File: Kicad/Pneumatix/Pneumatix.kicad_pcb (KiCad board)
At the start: 2 copper layers, 34 x 59.4 mm, 25 parts, among them J1 Conn_01x06_Socket, J2 436500404, J3 142-0701-801, U1 E22-400T33S

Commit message: wip: pcb adjustements
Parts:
- removed R1: 1.5k, Resistor_SMD:R_0603_1608Metric
- added C3: 100uF, Capacitor_SMD:C_0603_1608Metric, F.Cu at (6.60, 50.5)
- moved R2 2.97 mm to (28.5, 42.5), turned to -90 degrees
- moved C1 1.41 mm to (9.91, 50.5)
- moved C2 1.41 mm to (8.26, 50.5)
- moved J2 1.07 mm to (23.9, 50.3)
- moved D2 0.25 mm to (3.10, 50.5)
- moved R9 0.18 mm to (4.83, 50.5)
- moved H2 0.15 mm to (30.2, 25.3)
- moved J1 0.15 mm to (30.2, 19.2)
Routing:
- net Net-(D1-A): track 7.12 -> 3.04 mm
- net GND: track 5.70 -> 2.44 mm, vias 40 -> 39
- net Net-(U1-AUX): track 5.52 -> 3.00 mm
- net +5V: track 109.3 -> 110.5 mm
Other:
- board text added: "Samuel Gagnon Victor Deschênes 10-2026 V1"
- board text removed: "Samuel Gagnon Victor Deschênes 09-2026 V1"

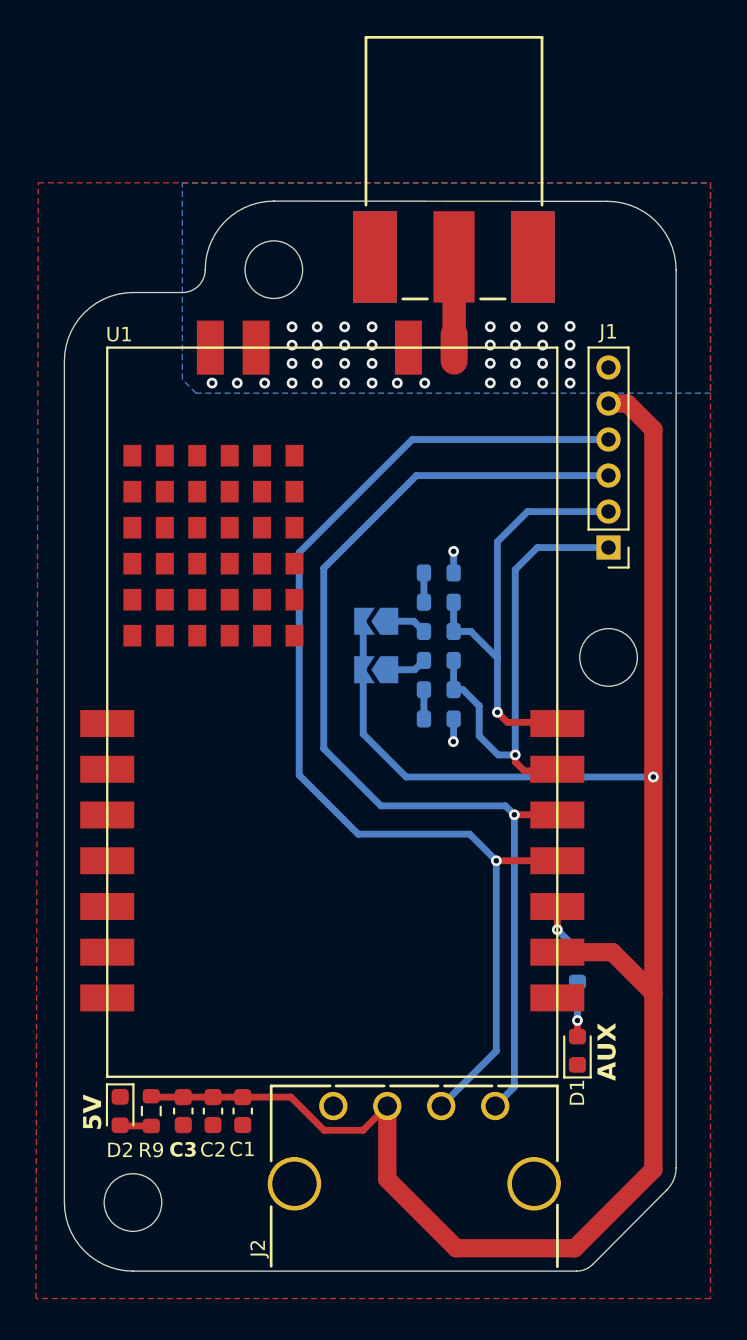
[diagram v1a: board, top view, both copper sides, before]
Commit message: wip: change 100uF cap to 220uF, add component fields and fix routing for new cap
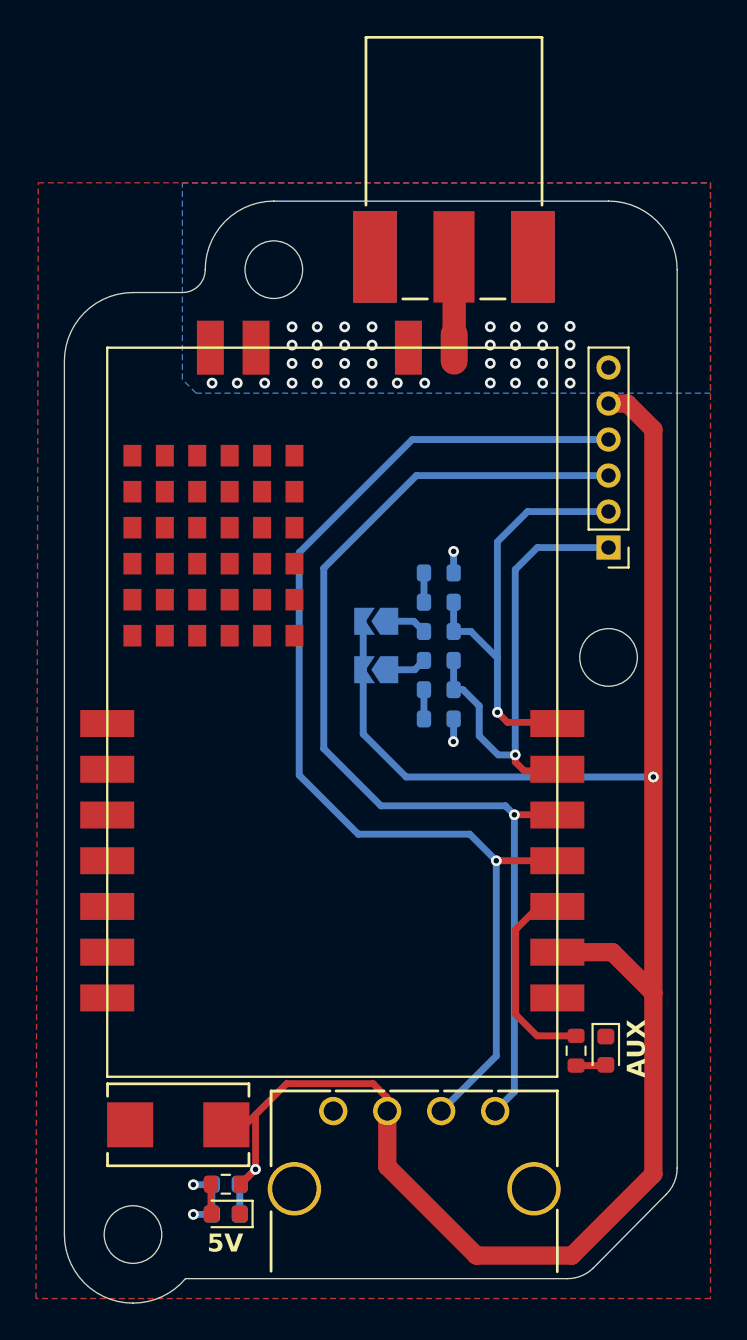
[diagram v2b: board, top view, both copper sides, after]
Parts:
- C1, C2: moved to B.Cu
- C3: value 100uF -> T520D227M010ATE018; footprint Capacitor_SMD:C_0603_1608Metric -> Pneumatix_Lib:CAPMP7.6X4.3_3.1N_KEM
- R2: moved to F.Cu
- moved D2 8.19 mm to (8.97, 56.3), turned to 180 degrees
- moved R9 5.80 mm to (8.97, 54.6), turned to 0 degrees
- moved C2 5.76 mm to (8.97, 56.3), turned to 180 degrees
- moved R2 4.65 mm to (28.4, 47.2)
- moved C1 4.17 mm to (8.97, 54.6), turned to 180 degrees
- moved H3 1.78 mm to (3.81, 57.4)
- moved D1 1.57 mm to (30.1, 47.2), turned to -90 degrees
- moved C3 0.81 mm to (6.32, 51.3), turned to 180 degrees
- moved J2 0.28 mm to (23.9, 50.5)
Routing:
- net Net-(U1-AUX): track 3.00 -> 10.4 mm, vias 1 -> 0
- net GND: track 2.44 -> 6.15 mm, vias 39 -> 41
- net +5V: track 110.5 -> 112.8 mm, vias 1 -> 2
- net Net-(D1-A): track 3.04 -> 1.61 mm, vias 1 -> 0
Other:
- board size 34 x 59.4 mm -> 34 x 61.2 mm
- board text added: "Pneumatix"
- board text removed: "Pneuamtix"
